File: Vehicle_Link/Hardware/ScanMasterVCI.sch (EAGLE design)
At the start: 80 parts, among them IC1 XMEGA32A4U, IC2 TL331, Q1 RUM002N05, Q10 ZXMP6A17G, Q3 RUM002N05, Q4 RUM002N05, Q5 RRF015P03, Q6 RUM002N05, Q7 RRF015P03, Q8 RRF015P03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

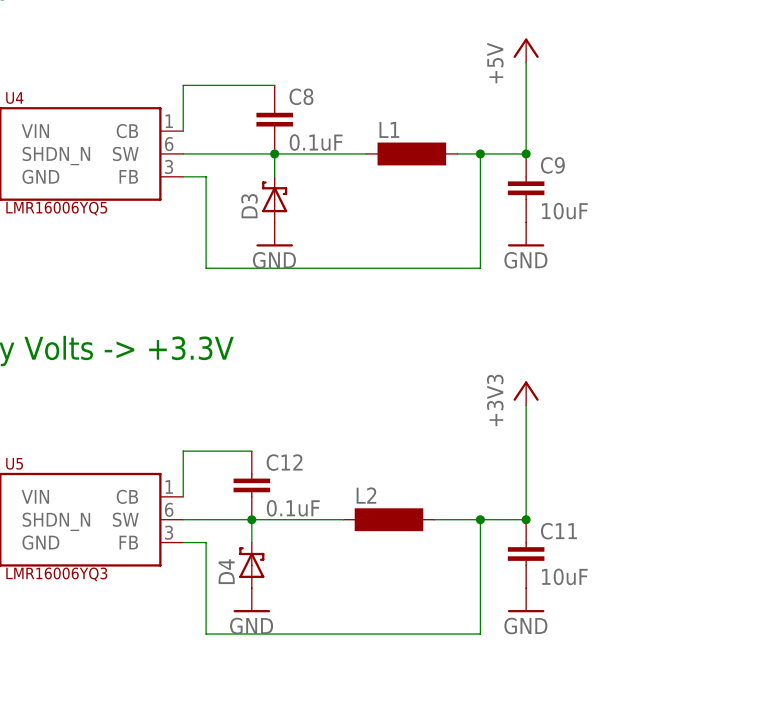
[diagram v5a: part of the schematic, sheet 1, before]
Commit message: Identified issues with top silkscreen layer.
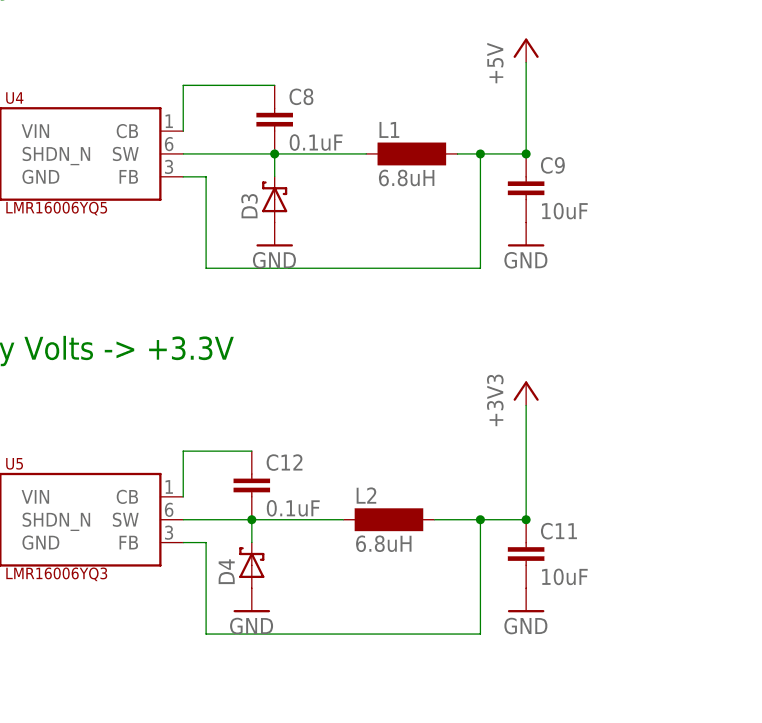
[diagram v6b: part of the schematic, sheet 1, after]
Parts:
- L1, L2: value (none) -> 6.8uH
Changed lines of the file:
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@@
 <part name="C11" library="SparkFun-Capacitors" library_urn="urn:adsk.eagle:library:510" deviceset="10UF" device="-0603-6.3V-20%" package3d_urn="urn:adsk.eagle:package:37414/1" value="10uF"/>
 <part name="C12" library="SparkFun-Capacitors" library_urn="urn:adsk.eagle:library:510" deviceset="0.1UF" device="-0603-25V-(+80/-20%)" package3d_urn="urn:adsk.eagle:package:37414/1" value="0.1uF"/>
-<part name="L1" library="inductor-neosid" library_urn="urn:adsk.eagle:library:241" deviceset="SM-1206" device="" package3d_urn="urn:adsk.eagle:package:14693/2"/>
-<part name="L2" library="inductor-neosid" library_urn="urn:adsk.eagle:library:241" deviceset="SM-1206" device="" package3d_urn="urn:adsk.eagle:package:14693/2"/>
+<part name="L1" library="inductor-neosid" library_urn="urn:adsk.eagle:library:241" deviceset="SM-1206" device="" package3d_urn="urn:adsk.eagle:package:14693/2" value="6.8uH"/>
+<part name="L2" library="inductor-neosid" library_urn="urn:adsk.eagle:library:241" deviceset="SM-1206" device="" package3d_urn="urn:adsk.eagle:package:14693/2" value="6.8uH"/>
 <part name="D3" library="customics" deviceset="SM5817PL" device=""/>
 <part name="D4" library="customics" deviceset="SM5817PL" device=""/>
